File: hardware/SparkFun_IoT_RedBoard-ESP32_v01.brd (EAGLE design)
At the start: 68.6 x 58.4 mm, 211 parts, among them J1 5.5x2.1mm Barrel, J13 QWIIC_RIGHT_ANGLE, J15 MICRO-SD-PUSH-PUSH-EXT-PIN, J2 USB C, J3 USB_SOLDER_PADS, J5 M10NO_SILK, Q1 MBT3904DW1T1, Q11 20V/4.2A/52mΩ/1.4W, Q13 20V/4.2A/52mΩ/1.4W, Q3 20V/4.2A/52mΩ/1.4W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

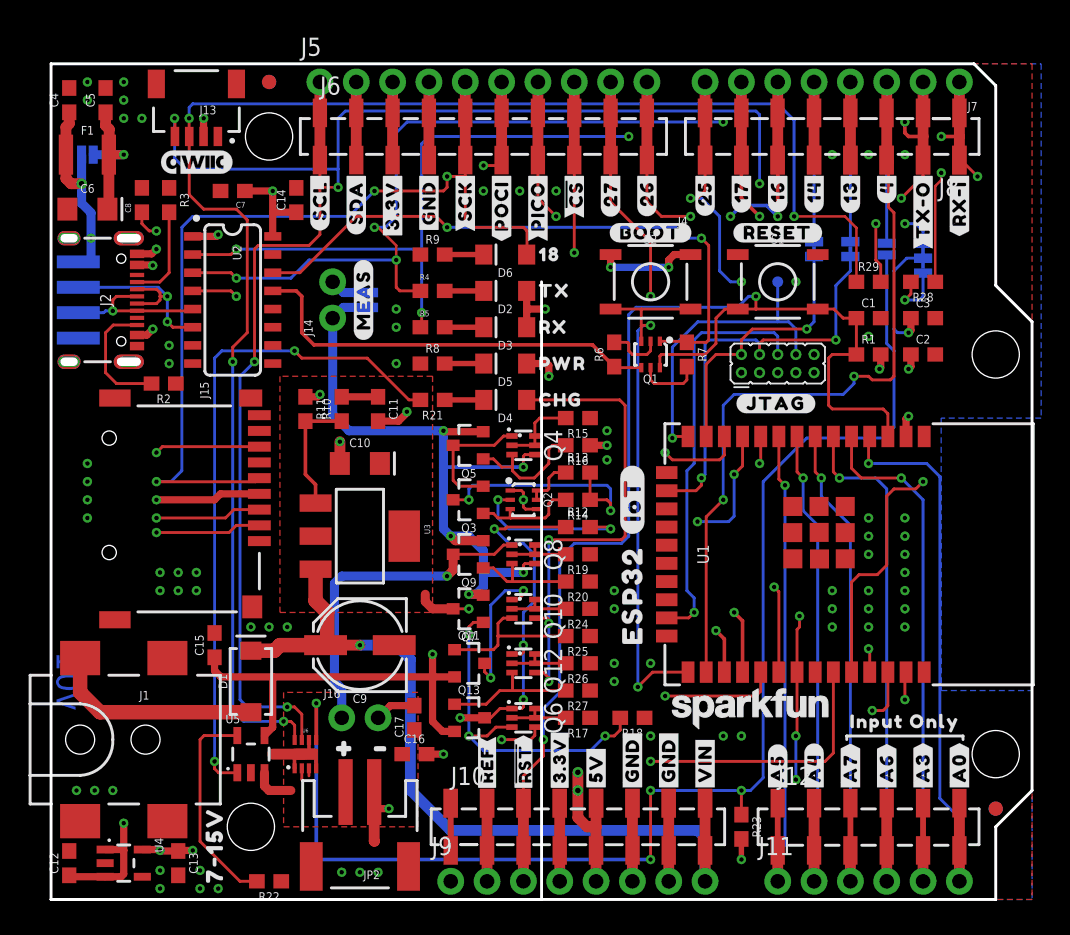
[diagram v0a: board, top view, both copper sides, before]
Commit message: Implemented changes suggested by Pete Lewis.
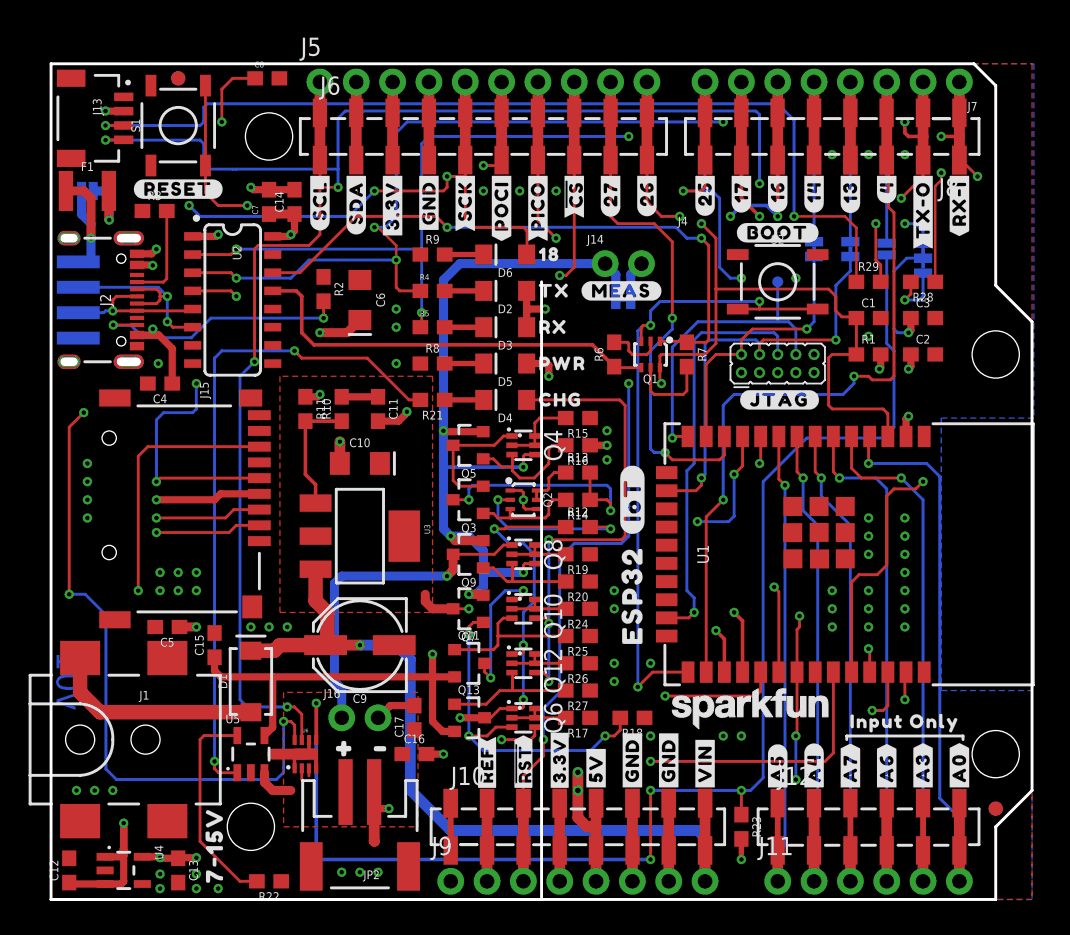
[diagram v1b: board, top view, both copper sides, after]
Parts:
- removed LOGO4: QWIIC_LOGO_5MM, SparkFun-Aesthetics:QWIIC_5MM
- added U$101: (no value), output-ESP32:7#15V32321861
- added U$103: (no value), output-ESP32:3#3V_LOGIC_SHIELDS_ONLY132321876
- moved FRAME1 102.6 mm to (19.6, -40.9)
- moved LOGO5 101.2 mm to (76.2, 58.4)
- moved S1 43.3 mm to (8.89, 54.1), turned to 90 degrees
- moved U$26 42.0 mm to (8.89, 49.7)
- moved C5 37.1 mm to (8.13, 19.1), turned to 180 degrees
- moved U$81 22.8 mm to (40.1, 46.4), turned to 0 degrees
- moved C4 20.8 mm to (7.62, 36.1), turned to 180 degrees
- moved C6 20.1 mm to (21.6, 41.9), turned to 270 degrees
- moved J14 19.4 mm to (38.7, 44.5), turned to 0 degrees
- moved U$42 18.0 mm to (39.9, 42.5), turned to 0 degrees
- moved JP10 17.8 mm to (40.0, 41.9), turned to 180 degrees
- moved R2 13.0 mm to (19.1, 42.7), turned to 270 degrees
- moved C8 12.2 mm to (15.1, 57.4), turned to 0 degrees
- moved LOGO2 9.16 mm to (1.52, 54.6), flipped to the bottom, turned to 90 degrees
- moved S2 8.89 mm to (50.8, 43.2)
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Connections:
- net VUSB renamed VBUS
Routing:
- net ESP32_EN: track 86.0 -> 125.4 mm, vias 2 -> 5
- net ESP32_SDA: track 163.0 -> 195.0 mm, vias 5 -> 6
- net 5V: track 110.6 -> 97.3 mm
- net CC2: track 8.75 -> 18.5 mm, vias 0 -> 2
- net ESP32_0: track 38.4 -> 46.7 mm, vias 2 -> 3
- net 5V_MEAS: track 64.6 -> 72.0 mm
- net N$6: track 14.4 -> 21.6 mm
- net V_USB: track 115.9 -> 120.4 mm, vias 5 -> 7
- net GND: track 50.6 -> 46.6 mm, vias 79 -> 71
- net ESP32_SCL: track 181.2 -> 184.7 mm
- net ESP32_GPIO27: track 33.3 -> 36.5 mm
- net ESP32_GPIO5_!CS!: track 112.4 -> 115.2 mm
- net ESP32_GPIO18_SCK: track 120.1 -> 122.3 mm, vias 4 -> 6
- net 3.3V: track 55.4 -> 53.5 mm
- net ESP32_GPIO25: track 33.3 -> 35.0 mm
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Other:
- board text added: "Dimensions in inches."

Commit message: Fixed silkscreen and via interference on bottom layer;
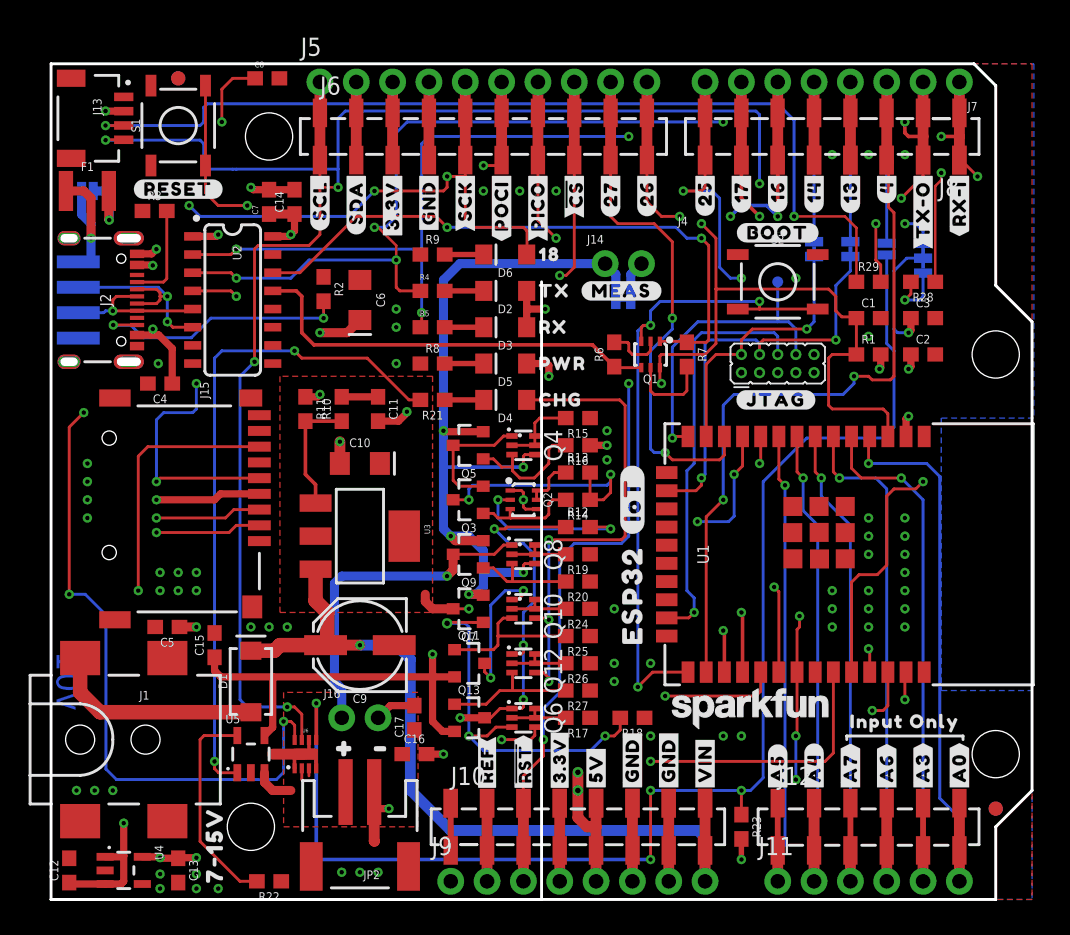
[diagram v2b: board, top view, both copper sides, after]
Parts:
- moved U$103 0.51 mm to (34.3, 18.5)
- moved U$28 0.25 mm to (50.7, 34.9)
- moved U$46 0.25 mm to (50.7, 34.9)
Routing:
- net N$10: track 24.5 -> 27.5 mm
- net 5V: track 97.3 -> 94.9 mm
- net GND: vias 71 -> 70

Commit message: Updated design per Engineering checklist.
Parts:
- moved U$28 0.76 mm to (51.4, 34.9)
- moved U$46 0.76 mm to (51.4, 34.9)
- moved J4 0.64 mm to (48.9, 36.8)
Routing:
- net ESP32_GPIO14_TMS: track 19.0 -> 20.8 mm
- net ESP32_EN: track 125.4 -> 123.8 mm
- net ESP32_RXD0: track 114.7 -> 116.1 mm
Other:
- board text added: "1"
- board text added: "2"
- board text added: "3"
- board text added: "4"
